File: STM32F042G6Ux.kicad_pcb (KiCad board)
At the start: 4 copper layers, 16 x 44.5 mm, 38 parts, among them J1 USB-TYPE-C-018, J2 FTSH-105-01-L-DV-K-TR, J3 Conn_ARM_SWD_TagConnect_TC203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, J4 2541WV-14P, J5 2541WV-14P, SW1 GT-TS171E-H014-L1, SW2 GT-TS171E-H014-L1, U1 USBLC6-2SC6, U2 STM32F042G6Ux, U3 DS8562-33S5

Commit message: DRC PASSgit add *
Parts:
- C3, C4, C5: footprint Capacitor_SMD:C_0402_1005Metric -> footprints:C_0402_1005Metric
- J1: footprint Connector_USB:USB_C_Receptacle_GCT_USB4105-xx-A_16P_TopMnt_Horizontal -> footprints:USB_C_Receptacle_GCT_USB4105-xx-A_16P_TopMnt_Horizontal
- JP1, JP2, JP3, JP4, JP5, R1, R2, R3, R4, R5, R6: footprint Resistor_SMD:R_0402_1005Metric -> footprints:R_0402_1005Metric
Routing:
- net GND: vias 19 -> 26

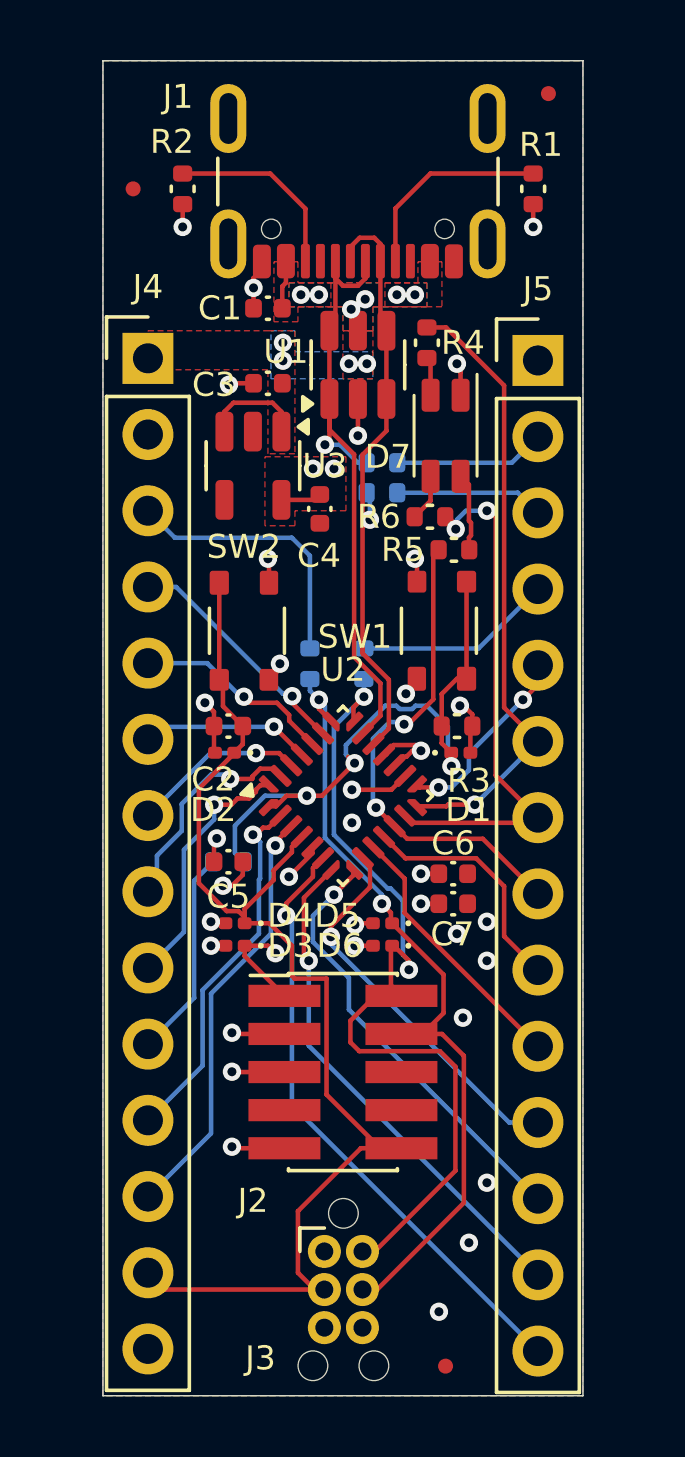
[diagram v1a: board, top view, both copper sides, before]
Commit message: centered usb port and via stitching
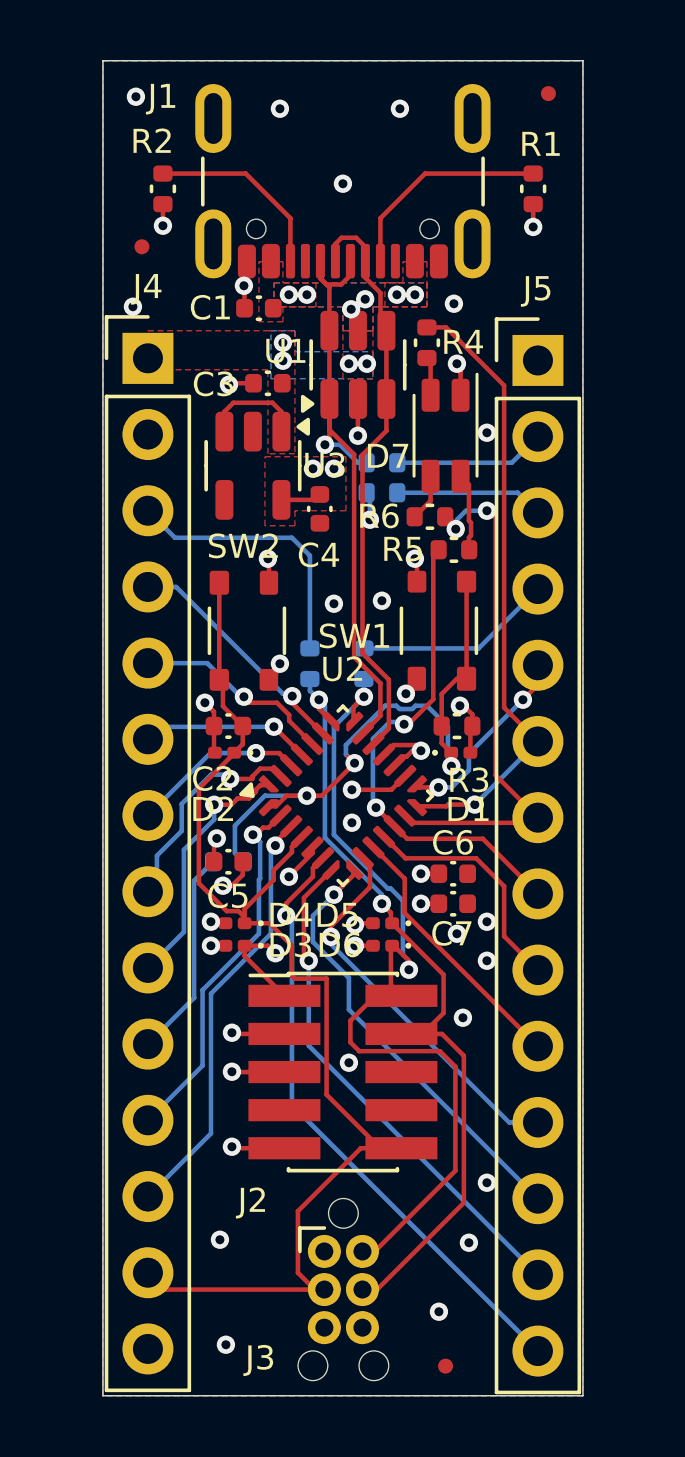
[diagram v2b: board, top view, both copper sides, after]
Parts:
- moved FID3 1.95 mm to (150.9, 90.6)
- moved R2 0.66 mm to (151.6, 88.7)
- moved J1 0.50 mm to (157.6, 87.4)
- moved C1 0.30 mm to (154.8, 92.6)
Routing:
- net VIN: track 5.09 -> 3.47 mm
- net /mcu/USB_DP: track 22.3 -> 21.7 mm
- net GND: track 20.7 -> 20.6 mm, vias 26 -> 38

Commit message: everything is broken
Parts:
- moved J5 0.09 mm to (164.1, 94.3)
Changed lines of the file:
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@@
 		(tags "capacitor")
 		(property "Reference" "C1"
-			(at 1.6 0 0)
+			(at 1.7 -0.05 0)
 			(unlocked yes)
 			(layer "F.SilkS")
@@
 		(tags "capacitor")
 		(property "Reference" "C3"
-			(at 1.8 -0.05 0)
+			(at 1 0.95 0)
 			(unlocked yes)
 			(layer "F.SilkS")
@@
 	(footprint "Connector_PinHeader_2.54mm:PinHeader_1x14_P2.54mm_Vertical"
 		(layer "F.Cu")
-		(at 164.11 94.385)
+		(at 164.1 94.295)
 		(descr "Through hole straight pin header, 1x14, 2.54mm pitch, single row")
 		(tags "Through hole pin header THT 1x14 2.54mm single row")
 		(property "Reference" "J5"
-			(at 0 -2.38 0)
+			(at 0.5 -2.29 0)
 			(unlocked yes)
 			(layer "F.SilkS")
@@
 		(tags "Through hole pin header THT 1x14 2.54mm single row")
 		(property "Reference" "J4"
-			(at 0 -2.38 0)
+			(at -0.4 -2.32 0)
 			(unlocked yes)
 			(layer "F.SilkS")
@@
 	)
 	(via
-		(at 162.41 96.795)
+		(at 162.11 96.795)
 		(size 0.61)
 		(drill 0.3)
@@
 			(pts
 				(xy 155.11 93.395) (xy 156.01 93.395) (xy 156.01 97.495) (xy 155.11 97.495) (xy 155.11 94.695) (xy 151.11 94.695)
-				(xy 151.11 93.395) (xy 155.11 93.395)
+				(xy 151.11 93.395)
 			)
 		)

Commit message: fixed everything
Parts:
- J4, J5: moved to B.Cu
- moved J4 1.17 mm to (150.0, 94.0), turned to 180 degrees
- moved J5 1.16 mm to (165.2, 94.0), turned to 180 degrees
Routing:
- net /mcu/PB0: track 20.6 -> 22.9 mm
- net /mcu/PA7: track 17.6 -> 19.9 mm
- net /mcu/PA13: track 6.62 -> 7.89 mm
- net /mcu/PA12: track 5.05 -> 6.32 mm
- net /mcu/PA15: track 8.00 -> 9.26 mm
- net /mcu/PA14: track 9.11 -> 10.4 mm
- net /mcu/PB3: track 6.71 -> 7.97 mm
- net /mcu/NRST: track 41.6 -> 42.9 mm
- net /mcu/PB5: track 5.81 -> 6.80 mm
- net /mcu/PB8: track 6.98 -> 7.98 mm
- net /mcu/PF1: track 14.4 -> 15.4 mm
- net /mcu/PF0: track 12.4 -> 13.4 mm
- net /mcu/PB7: track 8.48 -> 9.48 mm
- net /mcu/PB4: track 5.69 -> 6.69 mm
- net /mcu/PA1: track 17.1 -> 18.1 mm
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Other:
- board size 16 x 44.5 mm -> 18.8 x 44.4 mm

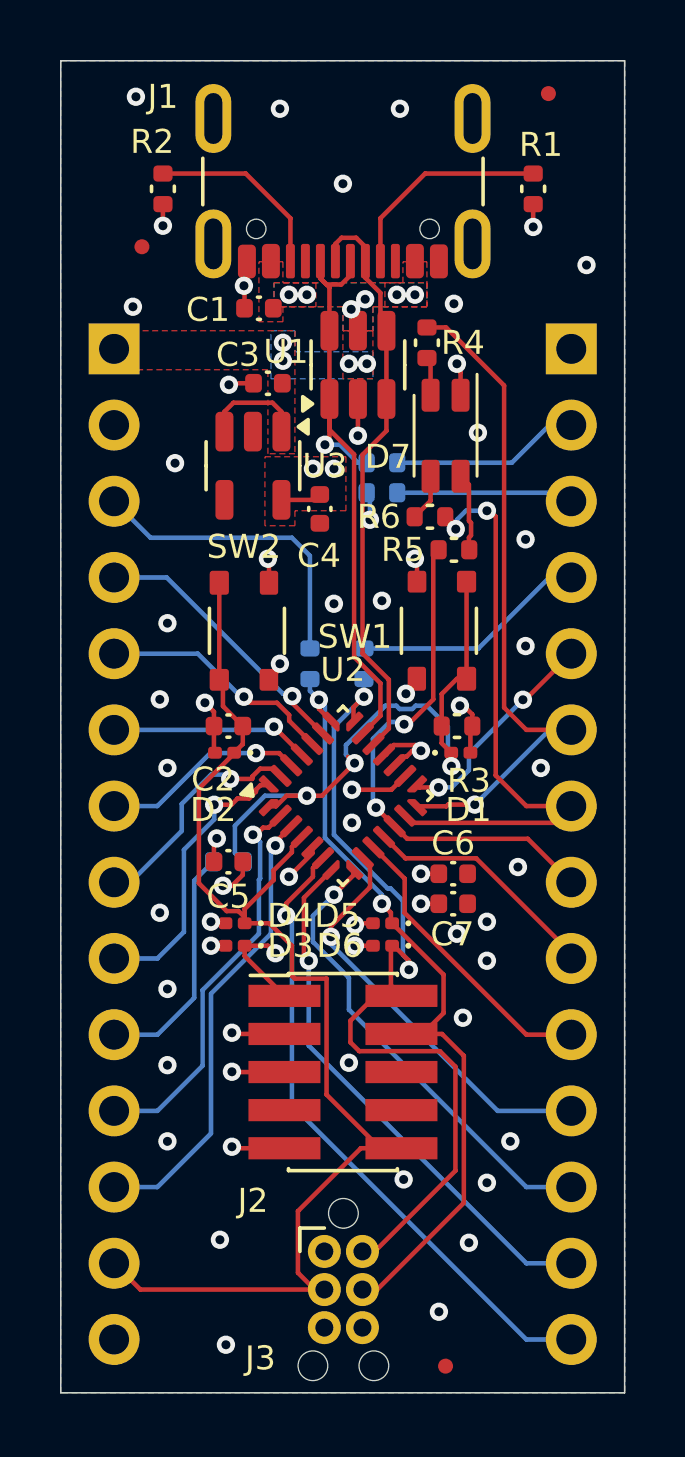
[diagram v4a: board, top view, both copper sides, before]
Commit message: pinout markings
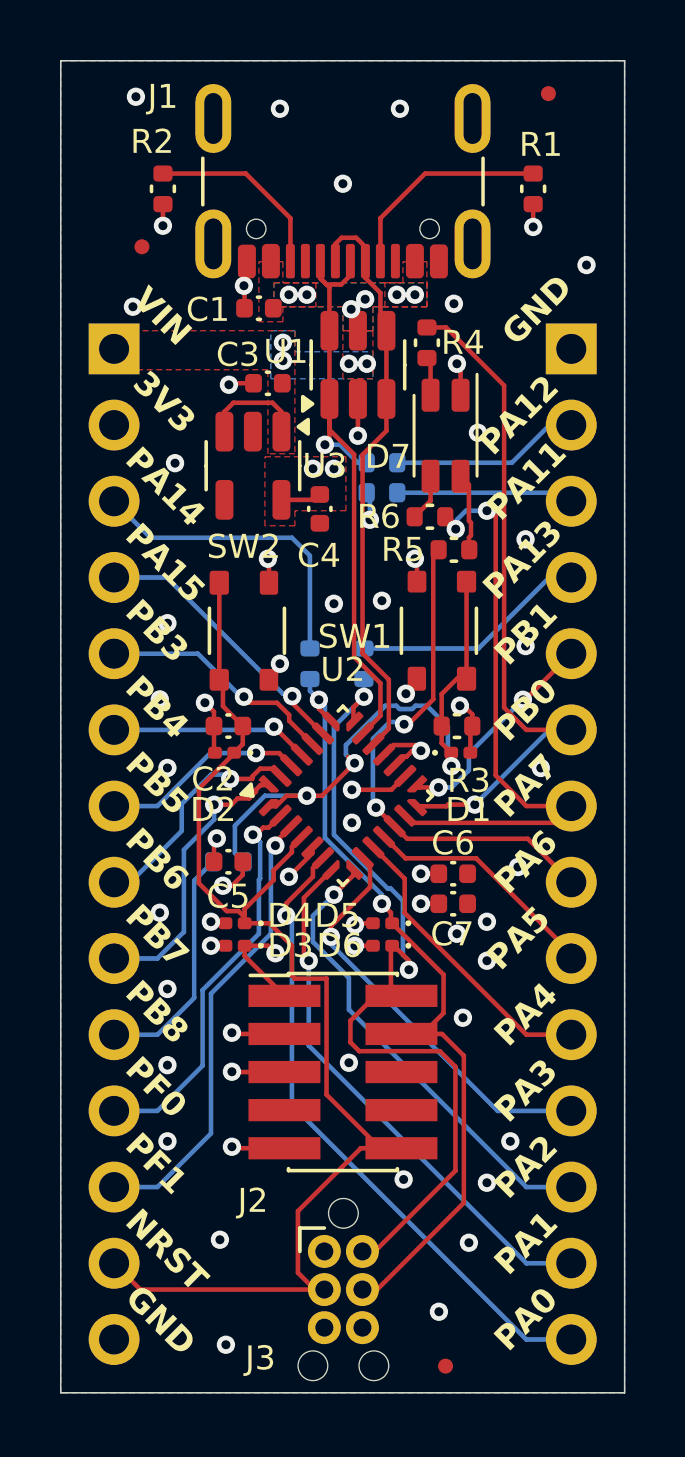
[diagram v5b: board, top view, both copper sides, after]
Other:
- board text added: "3V3"
- board text added: "GND"
- board text added: "NRST"
- board text added: "PA0"
- board text added: "PA1"
- board text added: "PA11"
- board text added: "PA12"
- board text added: "PA13"
- board text added: "PA14"
- board text added: "PA15"
- board text added: "PA2"
- board text added: "PA3"
- board text added: "PA4"
- board text added: "PA5"
- board text added: "PA6"
- board text added: "PA7"
- board text added: "PB0"
- board text added: "PB1"
- board text added: "PB3"
- board text added: "PB4"
- board text added: "PB5"
- board text added: "PB6"
- board text added: "PB7"
- board text added: "PB8"
- board text added: "PF0"
- board text added: "PF1"
- board text added: "VIN"

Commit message: bottom silk screen
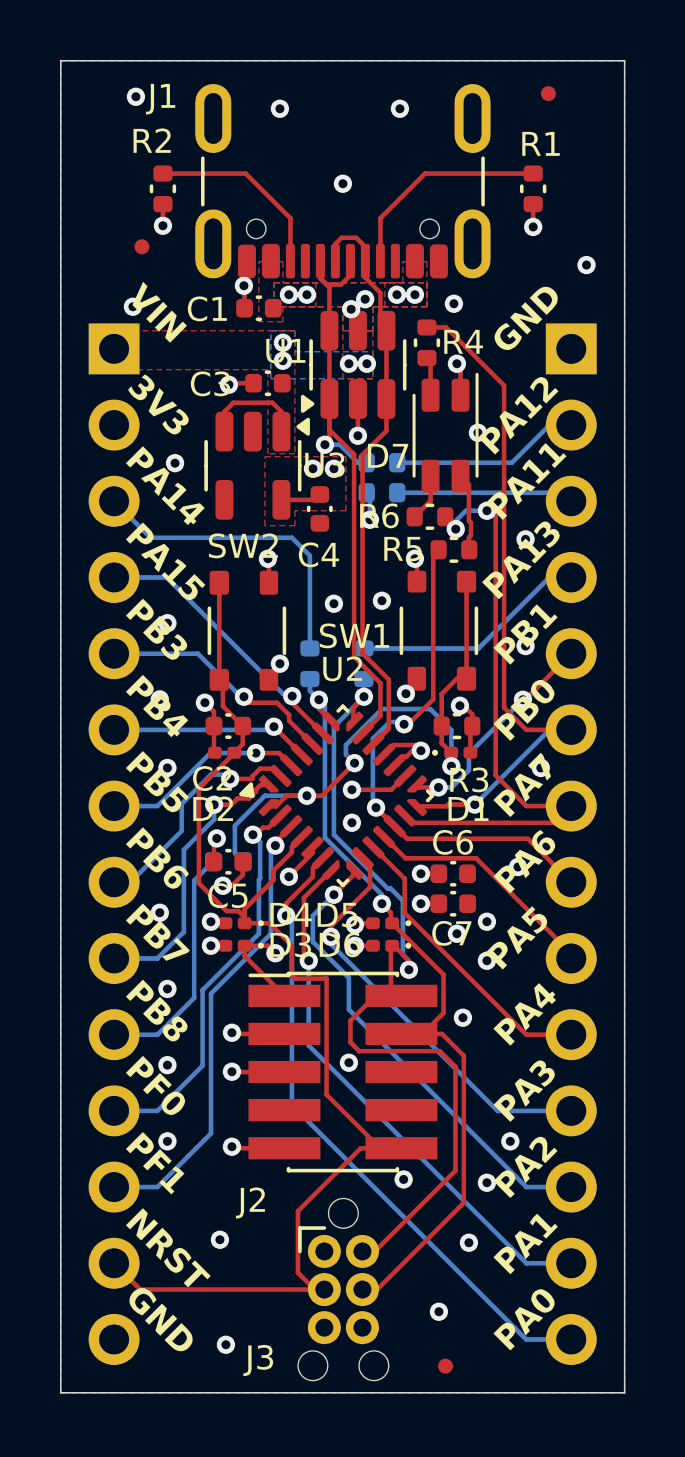
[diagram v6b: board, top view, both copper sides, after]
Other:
- board text added: "BOOT0 to PB8"
- board text added: "MCUEvalBoard_STM32F042G6Ux v1.0.0 by EmileBV"
- board text added: "SWCLK to PA14"
- board text added: "SWIO to PA13"
- board text added: "USB D+ to PA12"
- board text added: "USB D- to PA12"
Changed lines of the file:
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@@
 		(tags "capacitor")
 		(property "Reference" "C3"
-			(at 1 0.95 0)
+			(at 1.9 -0.05 0)
 			(unlocked yes)
 			(layer "F.SilkS")
@@
 		(tags "resistor")
 		(property "Reference" "JP3"
-			(at 0 1.1 0)
+			(at 2 0 0)
 			(unlocked yes)
 			(layer "B.SilkS")
@@
 		(tags "resistor")
 		(property "Reference" "JP2"
-			(at 0 -1 0)
+			(at 2 0 0)
 			(unlocked yes)
 			(layer "B.SilkS")
@@
 	)
 	(gr_text "VIN"
-		(at 150.49 92.475 315)
+		(at 150.31 92.395 315)
 		(layer "F.SilkS")
 		(effects
@@
 	)
 	(gr_text "GND"
-		(at 163.444 93.999 45)
+		(at 163.11 94.295 45)
 		(layer "F.SilkS")
 		(effects
@@
 	)
 	(gr_text "3V3"
-		(at 150.49 95.269 315)
+		(at 150.31 95.395 315)
 		(layer "F.SilkS")
 		(effects
@@
 		)
 	)
+	(gr_text "SWCLK\nto PA14"
+		(at 154.61 107.795 0)
+		(layer "B.SilkS")
+		(effects
+			(font
+				(size 0.8 0.8)
+				(thickness 0.15)
+				(bold yes)
+			)
+			(justify bottom mirror)
+		)
+	)
+	(gr_text "USB D+\nto PA12"
+		(at 158.91 97.095 0)
+		(layer "B.SilkS")
+		(effects
+			(font
+				(size 0.8 0.8)
+				(thickness 0.15)
+				(bold yes)
+			)
+			(justify bottom mirror)
+		)
+	)
+	(gr_text "SWIO\nto PA13"
+		(at 160.11 107.795 0)
+		(layer "B.SilkS")
+		(effects
+			(font
+				(size 0.8 0.8)
+				(thickness 0.15)
+				(bold yes)
+			)
+			(justify bottom mirror)
+		)
+	)
+	(gr_text "BOOT0\nto PB8"
+		(at 153.81 113.995 0)
+		(layer "B.SilkS")
+		(effects
+			(font
+				(size 0.8 0.8)
+				(thickness 0.15)
+				(bold yes)
+			)
+			(justify bottom mirror)
+		)
+	)
+	(gr_text "USB D-\nto PA12"
+		(at 158.91 101.595 0)
+		(layer "B.SilkS")
+		(effects
+			(font
+				(size 0.8 0.8)
+				(thickness 0.15)
+				(bold yes)
+			)
+			(justify bottom mirror)
+		)
+	)
+	(gr_text "MCUEvalBoard_STM32F042G6Ux\nv1.0.0\nby EmileBV"
+		(at 159.71 128.095 270)
+		(layer "B.SilkS")
+		(effects
+			(font
+				(size 0.8 0.8)
+				(thickness 0.15)
+				(bold yes)
+			)
+			(justify left bottom mirror)
+		)
+	)
 	(segment
 		(start 158.86 91.075)
@@
 	)
 	(segment
-		(start 157.71 107.520541)
-		(end 157.998423 107.808964)
-		(width 0.1524)
-		(layer "B.Cu")
-		(net 6)
-	)
-	(segment
-		(start 155.01 108.895)
-		(end 154.01 109.895)
-		(width 0.1524)
-		(layer "B.Cu")
-		(net 6)
-	)
-	(segment
-		(start 159.389882 105.895)
-		(end 159.022008 105.895)
-		(width 0.1524)
-		(layer "B.Cu")
-		(net 6)
-	)
-	(segment
-		(start 159.499082 106.0042)
-		(end 159.389882 105.895)
+		(start 161.224646 106.709646)
+		(end 160.5192 106.0042)
 		(width 0.1524)
 		(layer "B.Cu")
@@
 	)
 	(segment
-		(start 161.224646 107.709646)
-		(end 161.11 107.595)
+		(start 157.71 107.207008)
+		(end 157.71 107.520541)
 		(width 0.1524)
 		(layer "B.Cu")
@@
 	)
 	(segment
-		(start 160.41 105.895)
-		(end 160.030118 105.895)
+		(start 155.01 108.895)
+		(end 154.01 109.895)
 		(width 0.1524)
 		(layer "B.Cu")
@@
 	)
 	(segment
-		(start 160.030118 105.895)
-		(end 159.920918 106.0042)
+		(start 157.71 107.520541)
+		(end 157.998423 107.808964)
 		(width 0.1524)
 		(layer "B.Cu")
@@
 	)
 	(segment
-		(start 157.71 107.207008)
-		(end 157.71 107.520541)
+		(start 158.912808 106.0042)
+		(end 157.71 107.207008)
 		(width 0.1524)
 		(layer "B.Cu")
@@
 	)
 	(segment
-		(start 159.022008 105.895)
-		(end 157.71 107.207008)
+		(start 161.224646 107.909642)
+		(end 161.224646 106.709646)
 		(width 0.1524)
 		(layer "B.Cu")
@@
 	)
 	(segment
-		(start 161.11 107.595)
-		(end 161.11 106.595)
-		(width 0.1524)
-		(layer "B.Cu")
-		(net 6)
-	)
-	(segment
-		(start 159.920918 106.0042)
-		(end 159.499082 106.0042)
+		(start 160.5192 106.0042)
+		(end 158.912808 106.0042)
 		(width 0.1524)
 		(layer "B.Cu")
@@
 	)
 	(segment
-		(start 161.224646 107.909642)
-		(end 161.224646 107.709646)
+		(start 156.41 108.895)
+		(end 155.01 108.895)
 		(width 0.1524)
 		(layer "B.Cu")
@@
 	)
 	(segment
-		(start 161.11 106.595)
-		(end 160.41 105.895)
+		(start 160.9642 116.1392)
+		(end 160.9642 114.8592)
 		(width 0.1524)
-		(layer "B.Cu")
-		(net 6)
+		(layer "F.Cu")
+		(net 12)
 	)
 	(segment
-		(start 156.41 108.895)
-		(end 155.01 108.895)
+		(start 156.81 105.695)
+		(end 156.81 105.995)
 		(width 0.1524)
-		(layer "B.Cu")
-		(net 6)
+		(layer "F.Cu")
+		(net 12)
 	)
 	(segment
-		(start 160.9642 116.1392)
-		(end 160.9642 114.8592)
+		(start 156.81 105.995)
+		(end 157.236894 106.421894)
 		(width 0.1524)
 		(layer "F.Cu")
@@
 	)
 	(segment
-		(start 157.236894 106.421894)
-		(end 157.258214 106.421894)
-		(width 0.1524)
-		(layer "F.Cu")
-		(net 12)
-	)
-	(segment
 		(start 159.56 116.835)
 		(end 160.2684 116.835)
@@
 	)
 	(segment
-		(start 160.2684 116.835)
-		(end 160.9642 116.1392)
+		(start 157.236894 106.421894)
+		(end 157.258214 106.421894)
 		(width 0.1524)
 		(layer "F.Cu")
@@
 	)
 	(segment
-		(start 156.81 105.995)
-		(end 157.236894 106.421894)
+		(start 160.2684 116.835)
+		(end 160.9642 116.1392)
 		(width 0.1524)
 		(layer "F.Cu")
@@
 		(net 12)
 	)
-	(segment
-		(start 156.81 105.695)
-		(end 156.81 105.995)
-		(width 0.1524)
-		(layer "F.Cu")
-		(net 12)
-	)
 	(via
 		(at 156.81 105.695)
@@
 	)
 	(segment
-		(start 156.51 105.395)
-		(end 156.51 105.005)
+		(start 156.81 105.695)
+		(end 156.51 105.395)
 		(width 0.1524)
 		(layer "B.Cu")
@@
 	)
 	(segment
-		(start 158.91 112.495)
-		(end 158.91 112.195)
+		(start 158.91 112.195)
+		(end 158.91 112.495)
 		(width 0.1524)
 		(layer "B.Cu")
@@
 	)
 	(segment
-		(start 157.01 110.295)
+		(start 156.81 105.695)
 		(end 157.01 105.895)
 		(width 0.1524)
@@
 	)
 	(segment
-		(start 157.01 105.895)
-		(end 156.81 105.695)
+		(start 156.51 105.395)
+		(end 156.51 105.005)
 		(width 0.1524)
 		(layer "B.Cu")
@@
 	)
 	(segment
-		(start 158.91 112.195)
+		(start 157.01 105.895)
 		(end 157.01 110.295)
 		(width 0.1524)
@@
 	)
 	(segment
-		(start 156.81 105.695)
-		(end 156.51 105.395)
+		(start 157.01 110.295)
+		(end 158.91 112.195)
 		(width 0.1524)
 		(layer "B.Cu")
